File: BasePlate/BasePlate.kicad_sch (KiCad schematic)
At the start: 1 part, among them U1 STM32F446RCTx

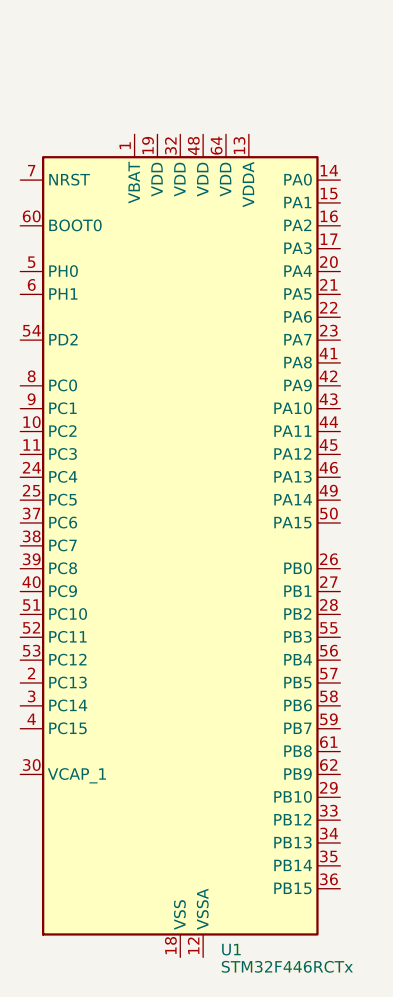
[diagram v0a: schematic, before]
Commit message: updated base-plate project and motor driver connections
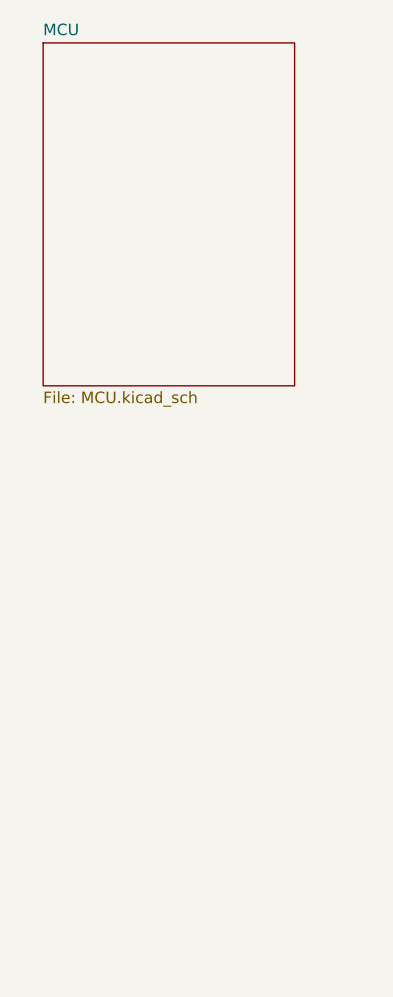
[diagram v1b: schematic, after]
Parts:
- removed U1: STM32F446RCTx, Package_QFP:LQFP-64_10x10mm_P0.5mm, symbol MCU_ST_STM32F4:STM32F446RCTx
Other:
- added sheet MCU (MCU.kicad_sch)
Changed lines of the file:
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@@
 (kicad_sch (version 20230121) (generator eeschema)
   (paper "A4")
-  (symbol (lib_id "MCU_ST_STM32F4:STM32F446RCTx") (at 66.04 93.98 0) (unit 1)
-    (in_bom yes) (on_board yes) (dnp no) (fields_autoplaced)
-    (property "Reference" "U1" (at 70.5359 138.8825 0)
-      (effects (font (size 1.27 1.27)) (justify left))
+  (sheet (at 50.8 38.1) (size 27.94 38.1) (fields_autoplaced)
+    (stroke (width 0.1524) (type solid))
+    (fill (color 0 132 0 0.5000))
+    (property "Sheetname" "MCU" (at 50.8 37.3884 0)
+      (effects (font (size 1.27 1.27)) (justify left bottom))
     )
-    (property "Value" "STM32F446RCTx" (at 70.5359 140.8035 0)
-      (effects (font (size 1.27 1.27)) (justify left))
+    (property "Sheetfile" "MCU.kicad_sch" (at 50.8 76.7846 0)
+      (effects (font (size 1.27 1.27)) (justify left top))
     )
-    (property "Footprint" "Package_QFP:LQFP-64_10x10mm_P0.5mm" (at 50.8 137.16 0)
-      (effects (font (size 1.27 1.27)) (justify right) hide)
-    )
-    (property "Datasheet" "https://www.st.com/resource/en/datasheet/stm32f446rc.pdf" (at 66.04 93.98 0)
+    (property "Field2" "" (at 50.8 38.1 0)
       (effects (font (size 1.27 1.27)) hide)
     )
-    (pin "1")
-    (pin "10")
-    (pin "11")
-    (pin "12")
-    (pin "13")
-    (pin "14")
-    (pin "15")
-    (pin "16")
-    (pin "17")
-    (pin "18")
-    (pin "19")
-    (pin "2")
-    (pin "20")
-    (pin "21")
-    (pin "22")
-    (pin "23")
-    (pin "24")
-    (pin "25")
-    (pin "26")
-    (pin "27")
-    (pin "28")
-    (pin "29")
-    (pin "3")
-    (pin "30")
-    (pin "31")
-    (pin "32")
-    (pin "33")
-    (pin "34")
-    (pin "35")
-    (pin "36")
-    (pin "37")
-    (pin "38")
-    (pin "39")
-    (pin "4")
-    (pin "40")
-    (pin "41")
-    (pin "42")
-    (pin "43")
-    (pin "44")
-    (pin "45")
-    (pin "46")
-    (pin "47")
-    (pin "48")
-    (pin "49")
-    (pin "5")
-    (pin "50")
-    (pin "51")
-    (pin "52")
-    (pin "53")
-    (pin "54")
-    (pin "55")
-    (pin "56")
-    (pin "57")
-    (pin "58")
-    (pin "59")
-    (pin "6")
-    (pin "60")
-    (pin "61")
-    (pin "62")
-    (pin "63")
-    (pin "64")
-    (pin "7")
-    (pin "8")
-    (pin "9")
     (instances
       (project "BasePlate"
-        (path "/30047588-8c40-4ef6-bedb-cb4a90042e6d"
-          (reference "U1") (unit 1)
-        )
+        (path "/30047588-8c40-4ef6-bedb-cb4a90042e6d" (page "2"))
       )
     )
